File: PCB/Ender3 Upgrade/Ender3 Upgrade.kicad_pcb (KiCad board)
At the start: 2 copper layers, 95.5 x 118.9 mm, 1 part

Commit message: LED Wire Clip
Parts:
- removed ?: BuckConverter, albe:BuckConverter
- added DCDCBC1: DCDCBuckConverter, albe:BuckConverter, F.Cu at (81.5, 120.1)
- added REF**: TerminalBlock_bornier-2_P5.08mm, TerminalBlock:TerminalBlock_bornier-2_P5.08mm, F.Cu at (111.3, 53.8)
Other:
- board size 95.5 x 118.9 mm -> 46 x 110.7 mm
- board text added: "24V"
- board text added: "GND"
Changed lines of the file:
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@@
   (general
     (thickness 1.6)
-    (drawings 18)
+    (drawings 14)
     (tracks 0)
     (zones 0)
-    (modules 1)
-    (nets 1)
+    (modules 2)
+    (nets 5)
   )
   (page A4)
@@
     (pad_drill 0.762)
     (pad_to_mask_clearance 0)
-    (aux_axis_origin 0 0)
-    (grid_origin 134.874 113.03)
-    (visible_elements FFFFFD7F)
+    (aux_axis_origin 18.796 151.638)
+    (grid_origin 43.942 185.166)
+    (visible_elements 7FFFFFFF)
     (pcbplotparams
       (layerselection 0x010fc_ffffffff)
@@
   )
   (net 0 "")
+  (net 1 "Net-(DCDCBC1-Pad4)")
+  (net 2 "Net-(DCDCBC1-Pad3)")
+  (net 3 +24V)
+  (net 4 GND)
   (net_class Default "This is the default net class."
     (clearance 0.2)
@@
     (uvia_dia 0.3)
     (uvia_drill 0.1)
+    (add_net +24V)
+    (add_net GND)
+    (add_net "Net-(DCDCBC1-Pad3)")
+    (add_net "Net-(DCDCBC1-Pad4)")
   )
   (module albe:BuckConverter (layer F.Cu)
-    (at 129.032 79.756)
-    (fp_text reference "" (at 0 -22.36) (layer F.SilkS)
-      (effects (font (size 1 1) (thickness 0.15)))
-    )
-    (fp_text value BuckConverter (at 0 -23.36) (layer F.Fab)
+    (at 81.534 120.142)
+    (fp_text reference DCDCBC1 (at 0 -22.36) (layer F.SilkS)
+      (effects (font (size 1 1) (thickness 0.15)))
+    )
+    (fp_text value DCDCBuckConverter (at 0 -23.36) (layer F.Fab)
       (effects (font (size 1 1) (thickness 0.15)))
     )
@@
     (fp_line (start 0 -10.16) (end 5.08 -5.08) (layer F.SilkS) (width 0.12))
     (fp_line (start 5.08 -5.08) (end 3.81 -5.08) (layer F.SilkS) (width 0.12))
-    (pad 4 thru_hole circle (at -8.939073 -19.398813) (size 2 2) (drill 0.762) (layers *.Cu *.Mask))
-    (pad 3 thru_hole circle (at 8.89 -19.398813) (size 2 2) (drill 0.762) (layers *.Cu *.Mask))
-    (pad 2 thru_hole circle (at -8.939073 20.801187) (size 2 2) (drill 0.762) (layers *.Cu *.Mask))
-    (pad 1 thru_hole circle (at 8.910927 20.801187) (size 2 2) (drill 0.762) (layers *.Cu *.Mask))
-  )
-  (gr_line (start 69.596 41.91) (end 84.665419 42.231605) (layer Edge.Cuts) (width 0.05))
-  (gr_line (start 69.596 160.782) (end 69.596 41.91) (layer Edge.Cuts) (width 0.05))
-  (gr_line (start 164.846 160.782) (end 69.596 160.782) (layer Edge.Cuts) (width 0.05))
-  (gr_line (start 165.146 160.782) (end 164.846 160.782) (layer Edge.Cuts) (width 0.05))
-  (gr_line (start 165.146 68.95) (end 165.146 160.782) (layer Edge.Cuts) (width 0.05))
-  (gr_circle (center 107.696 94.5) (end 106.296 94.5) (layer Dwgs.User) (width 0.2))
-  (gr_arc (start 150.146 145.95) (end 150.146 160.95) (angle -18.1761416) (layer Dwgs.User) (width 0.2))
-  (gr_line (start 84.665419 160.95) (end 150.146 160.95) (layer Dwgs.User) (width 0.2))
-  (gr_arc (start 84.665419 145.95) (end 69.665419 145.95) (angle -90) (layer Dwgs.User) (width 0.2))
-  (gr_arc (start 84.665419 57.231605) (end 84.665419 42.231605) (angle -90) (layer Dwgs.User) (width 0.2))
-  (gr_line (start 150.146 42.231605) (end 84.665419 42.231605) (layer Edge.Cuts) (width 0.2))
-  (gr_line (start 168.146 68.95) (end 165.146 68.95) (layer Dwgs.User) (width 0.2))
-  (gr_circle (center 156.596 94.5) (end 155.196 94.5) (layer Dwgs.User) (width 0.2))
-  (gr_circle (center 156.596 152.4) (end 155.196 152.4) (layer Dwgs.User) (width 0.2))
-  (gr_arc (start 150.146 57.231605) (end 165.146 57.231605) (angle -90) (layer Edge.Cuts) (width 0.2))
-  (gr_line (start 165.146 68.95) (end 165.146 57.231605) (layer Edge.Cuts) (width 0.2))
-  (gr_line (start 69.665419 57.231605) (end 69.665419 145.95) (layer Dwgs.User) (width 0.2))
-  (gr_circle (center 107.696 152.4) (end 106.296 152.4) (layer Dwgs.User) (width 0.2))
+    (pad 4 thru_hole circle (at -8.939073 -19.398813) (size 2 2) (drill 0.762) (layers *.Cu *.Mask)
+      (net 1 "Net-(DCDCBC1-Pad4)"))
+    (pad 3 thru_hole circle (at 8.89 -19.398813) (size 2 2) (drill 0.762) (layers *.Cu *.Mask)
+      (net 2 "Net-(DCDCBC1-Pad3)"))
+    (pad 2 thru_hole circle (at -8.939073 20.801187) (size 2 2) (drill 0.762) (layers *.Cu *.Mask)
+      (net 3 +24V))
+    (pad 1 thru_hole circle (at 8.910927 20.801187) (size 2 2) (drill 0.762) (layers *.Cu *.Mask)
+      (net 4 GND))
+  )
+  (module TerminalBlock:TerminalBlock_bornier-2_P5.08mm (layer F.Cu)
+    (at 111.252 53.848 90)
+    (descr "simple 2-pin terminal block, pitch 5.08mm, revamped version of bornier2")
+    (tags "terminal block bornier2")
+    (fp_text reference REF** (at 2.54 -5.08 90) (layer F.SilkS)
+      (effects (font (size 1 1) (thickness 0.15)))
+    )
+    (fp_text value TerminalBlock_bornier-2_P5.08mm (at 2.54 5.08 90) (layer F.Fab)
+      (effects (font (size 1 1) (thickness 0.15)))
+    )
+    (fp_text user %R (at 2.54 0 90) (layer F.Fab)
+      (effects (font (size 1 1) (thickness 0.15)))
+    )
+    (fp_line (start -2.41 2.55) (end 7.49 2.55) (layer F.Fab) (width 0.1))
+    (fp_line (start -2.46 -3.75) (end -2.46 3.75) (layer F.Fab) (width 0.1))
+    (fp_line (start -2.46 3.75) (end 7.54 3.75) (layer F.Fab) (width 0.1))
+    (fp_line (start 7.54 3.75) (end 7.54 -3.75) (layer F.Fab) (width 0.1))
+    (fp_line (start 7.54 -3.75) (end -2.46 -3.75) (layer F.Fab) (width 0.1))
+    (fp_line (start 7.62 2.54) (end -2.54 2.54) (layer F.SilkS) (width 0.12))
+    (fp_line (start 7.62 3.81) (end 7.62 -3.81) (layer F.SilkS) (width 0.12))
+    (fp_line (start 7.62 -3.81) (end -2.54 -3.81) (layer F.SilkS) (width 0.12))
+    (fp_line (start -2.54 -3.81) (end -2.54 3.81) (layer F.SilkS) (width 0.12))
+    (fp_line (start -2.54 3.81) (end 7.62 3.81) (layer F.SilkS) (width 0.12))
+    (fp_line (start -2.71 -4) (end 7.79 -4) (layer F.CrtYd) (width 0.05))
+    (fp_line (start -2.71 -4) (end -2.71 4) (layer F.CrtYd) (width 0.05))
+    (fp_line (start 7.79 4) (end 7.79 -4) (layer F.CrtYd) (width 0.05))
+    (fp_line (start 7.79 4) (end -2.71 4) (layer F.CrtYd) (width 0.05))
+    (pad 2 thru_hole circle (at 5.08 0 90) (size 3 3) (drill 1.52) (layers *.Cu *.Mask))
+    (pad 1 thru_hole rect (at 0 0 90) (size 3 3) (drill 1.52) (layers *.Cu *.Mask))
+    (model ${KISYS3DMOD}/TerminalBlock.3dshapes/TerminalBlock_bornier-2_P5.08mm.wrl
+      (offset (xyz 2.539999961853027 0 0))
+      (scale (xyz 1 1 1))
+      (rotate (xyz 0 0 0))
+    )
+  )
+  (gr_line (start 70.026 141.374395) (end 70.026 52.656) (layer Edge.Cuts) (width 0.2))
+  (gr_arc (start 81.026 52.656) (end 81.026 41.656) (angle -90) (layer Edge.Cuts) (width 0.2))
+  (gr_text 24V (at 111.506 57.658) (layer F.SilkS)
+    (effects (font (size 1 1) (thickness 0.15)))
+  )
+  (gr_text GND (at 111.252 44.704) (layer F.SilkS)
+    (effects (font (size 1 1) (thickness 0.15)))
+  )
+  (gr_arc (start 114.026 43.656) (end 116.026 43.656) (angle -90) (layer Edge.Cuts) (width 0.2))
+  (gr_arc (start 86.026 147.374395) (end 86.026 152.374395) (angle -90) (layer Edge.Cuts) (width 0.2))
+  (gr_line (start 111.026 77.374395) (end 96.026 77.374395) (layer Edge.Cuts) (width 0.2))
+  (gr_line (start 116.026 43.656) (end 116.026 72.374395) (layer Edge.Cuts) (width 0.2))
+  (gr_line (start 91.026 82.374395) (end 91.026 147.374395) (layer Edge.Cuts) (width 0.2))
+  (gr_arc (start 81.026 141.374395) (end 70.026 141.374395) (angle -90) (layer Edge.Cuts) (width 0.2))
+  (gr_line (start 86.026 152.374395) (end 81.026 152.374395) (layer Edge.Cuts) (width 0.2))
+  (gr_arc (start 96.026 82.374395) (end 96.026 77.374395) (angle -90) (layer Edge.Cuts) (width 0.2))
+  (gr_arc (start 111.026 72.374395) (end 111.026 77.374395) (angle -90) (layer Edge.Cuts) (width 0.2))
+  (gr_line (start 81.026 41.656) (end 114.026 41.656) (layer Edge.Cuts) (width 0.2))
 )

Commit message: PCB Designed
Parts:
- removed the REF** at (111.3, 53.8)
- added C1: Conn_01x02, Connector_JST:JST_EH_B2B-EH-A_1x02_P2.50mm_Vertical, F.Cu at (131.8, 100.2)
- added C2: Conn_01x02, Connector_JST:JST_EH_B2B-EH-A_1x02_P2.50mm_Vertical, F.Cu at (160.3, 100.4)
- added C3: Conn_01x02, Connector_JST:JST_EH_B2B-EH-A_1x02_P2.50mm_Vertical, F.Cu at (143.7, 100.2)
- added C4: Conn_01x02, Connector_JST:JST_EH_B2B-EH-A_1x02_P2.50mm_Vertical, F.Cu at (172.2, 100.4)
- added C5: Conn_01x02, Connector_JST:JST_EH_B2B-EH-A_1x02_P2.50mm_Vertical, F.Cu at (141.2, 126.8)
- added C6: Conn_01x02, Connector_JST:JST_EH_B2B-EH-A_1x02_P2.50mm_Vertical, F.Cu at (169.7, 126.8)
- added C7: Conn_01x02, Connector_JST:JST_EH_B2B-EH-A_1x02_P2.50mm_Vertical, F.Cu at (129.3, 126.8)
- added C8: Conn_01x02, Connector_JST:JST_EH_B2B-EH-A_1x02_P2.50mm_Vertical, F.Cu at (157.7, 126.8)
- added DCDCBC2: DCDC 24-12, albe:BuckConverter, F.Cu at (99.8, 122.0)
- added J1 5V: Conn_01x04_Male, Connector_PinSocket_2.54mm:PinSocket_1x04_P2.54mm_Vertical, F.Cu at (140.2, 90.5)
- added J2 12V: Conn_01x04_Male, Connector_PinSocket_2.54mm:PinSocket_1x04_P2.54mm_Vertical, F.Cu at (161.0, 90.2)
- added R1: R1, Resistor_THT:R_Axial_DIN0204_L3.6mm_D1.6mm_P7.62mm_Horizontal, F.Cu at (126.7, 111.3)
- added R2: R1, Resistor_THT:R_Axial_DIN0204_L3.6mm_D1.6mm_P7.62mm_Horizontal, F.Cu at (155.2, 111.6)
- added R3: R1, Resistor_THT:R_Axial_DIN0204_L3.6mm_D1.6mm_P7.62mm_Horizontal, F.Cu at (138.7, 111.3)
- added R4: R1, Resistor_THT:R_Axial_DIN0204_L3.6mm_D1.6mm_P7.62mm_Horizontal, F.Cu at (167.1, 111.6)
- added R5: R1, Resistor_THT:R_Axial_DIN0204_L3.6mm_D1.6mm_P7.62mm_Horizontal, F.Cu at (146.3, 115.6)
- added R6: R1, Resistor_THT:R_Axial_DIN0204_L3.6mm_D1.6mm_P7.62mm_Horizontal, F.Cu at (174.7, 115.9)
- added R7: R1, Resistor_THT:R_Axial_DIN0204_L3.6mm_D1.6mm_P7.62mm_Horizontal, F.Cu at (134.3, 115.6)
- added R8: R1, Resistor_THT:R_Axial_DIN0204_L3.6mm_D1.6mm_P7.62mm_Horizontal, F.Cu at (162.8, 115.9)
- added REF**: MountingHole_2.2mm_M2_Pad, MountingHole:MountingHole_2.2mm_M2_Pad, F.Cu at (176.9, 87.9)
- added REF**: MountingHole_2.2mm_M2_Pad, MountingHole:MountingHole_2.2mm_M2_Pad, F.Cu at (176.7, 131.5)
- added REF**: MountingHole_2.2mm_M2_Pad, MountingHole:MountingHole_2.2mm_M2_Pad, F.Cu at (73.1, 131.6)
- added REF**: MountingHole_2.2mm_M2_Pad, MountingHole:MountingHole_2.2mm_M2_Pad, F.Cu at (73.4, 88.0)
- added T1: IRLZ34N, Package_TO_SOT_THT:TO-220-3_Vertical, F.Cu at (128.0, 107.2)
- added T2: IRLZ34N, Package_TO_SOT_THT:TO-220-3_Vertical, F.Cu at (156.5, 107.5)
- added T3: IRLZ34N, Package_TO_SOT_THT:TO-220-3_Vertical, F.Cu at (140.0, 107.2)
- added T4: IRLZ34N, Package_TO_SOT_THT:TO-220-3_Vertical, F.Cu at (168.4, 107.5)
- added T5: IRLZ34N, Package_TO_SOT_THT:TO-220-3_Vertical, F.Cu at (145.0, 119.8)
- added T6: IRLZ34N, Package_TO_SOT_THT:TO-220-3_Vertical, F.Cu at (173.4, 119.9)
- added T7: IRLZ34N, Package_TO_SOT_THT:TO-220-3_Vertical, F.Cu at (133.1, 119.8)
- added T8: IRLZ34N, Package_TO_SOT_THT:TO-220-3_Vertical, F.Cu at (161.5, 119.9)
- DCDCBC1: value DCDCBuckConverter -> DCDC 24-5
- moved DCDCBC1 28.8 mm to (99.8, 97.9), turned to 270 degrees
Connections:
- DCDCBC1 pad 1: GND -> GNDPWR
- DCDCBC1 pad 3: Net-(DCDCBC1-Pad3) -> GND
- DCDCBC1 pad 4: Net-(DCDCBC1-Pad4) -> 5V
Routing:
- net GND: track 0.00 -> 124.7 mm
- net 12V: track 0.00 -> 116.0 mm
- net 5V: track 0.00 -> 73.6 mm
- net Net-(J1-Pad1): track 0.00 -> 73.5 mm
- net Net-(J2-Pad4): track 0.00 -> 71.5 mm
- net Net-(J1-Pad2): track 0.00 -> 35.5 mm
- net Net-(J2-Pad3): track 0.00 -> 35.0 mm
- net +24V: track 0.00 -> 27.5 mm
- net GNDPWR: track 0.00 -> 27.5 mm
- net Net-(J2-Pad2): track 0.00 -> 23.9 mm
- net Net-(J2-Pad1): track 0.00 -> 23.7 mm
- net Net-(J1-Pad3): track 0.00 -> 23.6 mm
- net Net-(J1-Pad4): track 0.00 -> 23.4 mm
- net Net-(C3-Pad1): track 0.00 -> 7.58 mm
- net Net-(C1-Pad1): track 0.00 -> 7.58 mm
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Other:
- board size 46 x 110.7 mm -> 110 x 50 mm
- board text added: "1"
- board text added: "12V"
- board text added: "2"
- board text added: "3"
- board text added: "4"
- board text added: "5"
- board text added: "5V"
- board text added: "6"
- board text added: "7"
- board text added: "8"
- board text added: "Ideated and Designed by Alberto Rota"
- board text removed: "24V"
- board text removed: "GND"

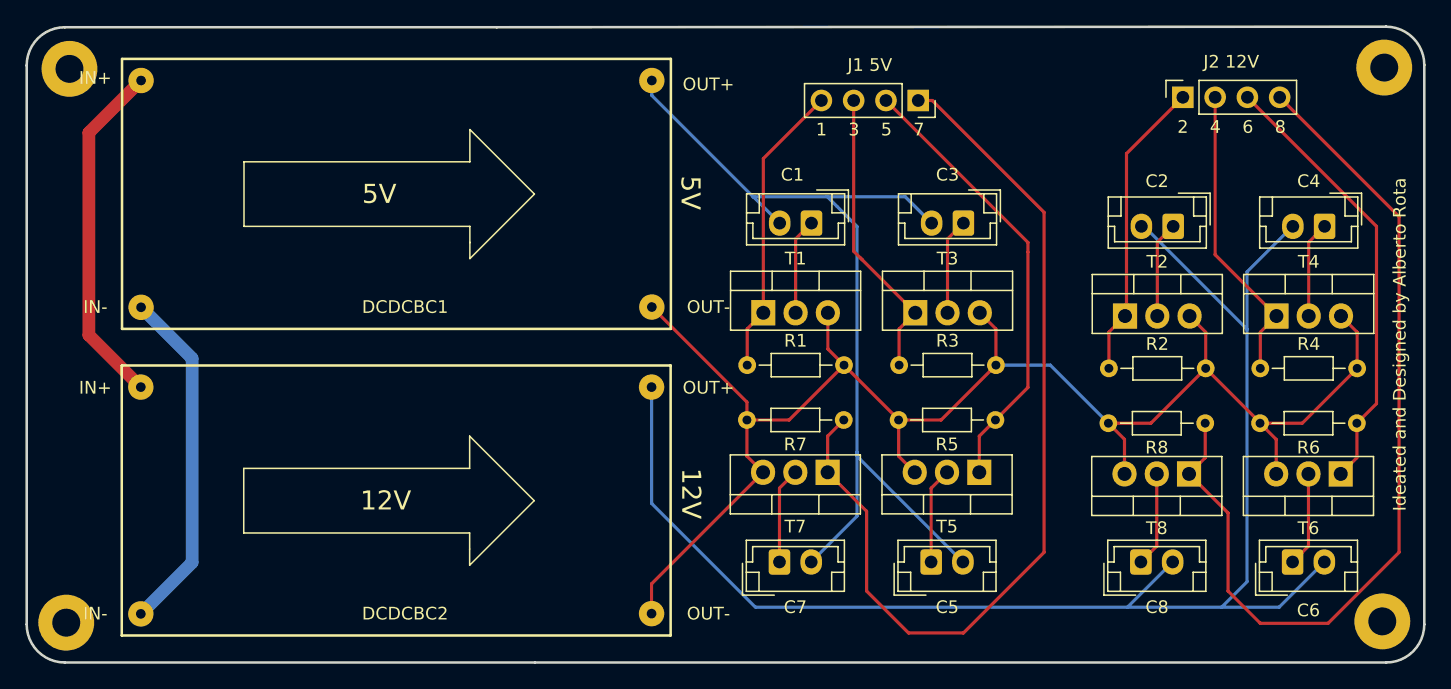
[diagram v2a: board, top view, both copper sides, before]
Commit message: Drawers added
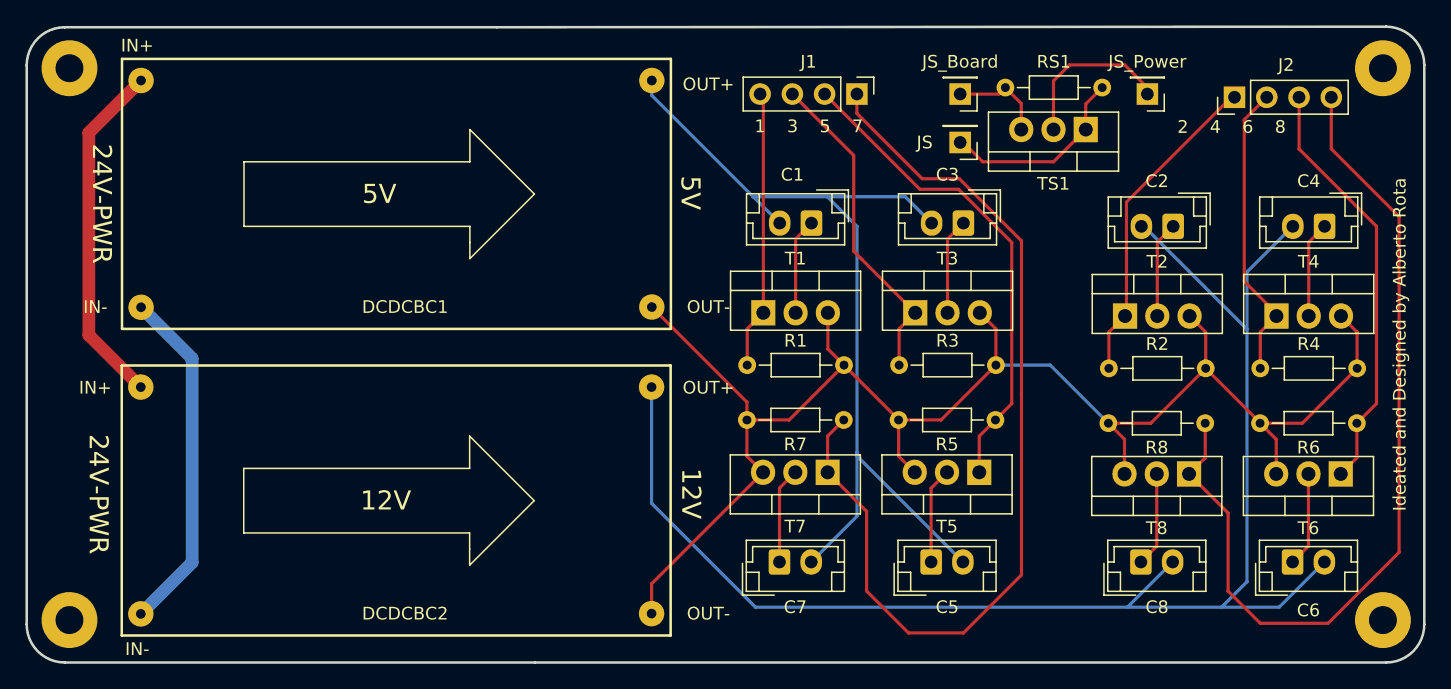
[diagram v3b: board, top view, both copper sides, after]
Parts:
- removed J1 5V: Conn_01x04_Male, Connector_PinSocket_2.54mm:PinSocket_1x04_P2.54mm_Vertical
- removed J2 12V: Conn_01x04_Male, Connector_PinSocket_2.54mm:PinSocket_1x04_P2.54mm_Vertical
- removed the REF** at (176.9, 87.9)
- removed the REF** at (176.7, 131.5)
- removed the REF** at (73.1, 131.6)
- added J1: Conn_01x04_Male, Connector_PinHeader_2.54mm:PinHeader_1x04_P2.54mm_Vertical, F.Cu at (135.4, 90.0)
- added J2: Conn_01x04_Male, Connector_PinHeader_2.54mm:PinHeader_1x04_P2.54mm_Vertical, F.Cu at (165.1, 90.2)
- added JS: Conn_01x01_Male, Connector_PinHeader_2.54mm:PinHeader_1x01_P2.54mm_Vertical, F.Cu at (143.5, 93.8)
- added JS_Board: Conn_01x01_Male, Connector_PinHeader_2.54mm:PinHeader_1x01_P2.54mm_Vertical, F.Cu at (143.5, 90.0)
- added JS_Power: Conn_01x01_Male, Connector_PinHeader_2.54mm:PinHeader_1x01_P2.54mm_Vertical, F.Cu at (158.2, 90.0)
- added REF**: MountingHole_2.2mm_M2_Pad, MountingHole:MountingHole_2.2mm_M2_Pad, F.Cu at (176.8, 88.0)
- added REF**: MountingHole_2.2mm_M2_Pad, MountingHole:MountingHole_2.2mm_M2_Pad, F.Cu at (176.8, 131.4)
- added REF**: MountingHole_2.2mm_M2_Pad, MountingHole:MountingHole_2.2mm_M2_Pad, F.Cu at (73.4, 131.4)
- added RS1: R1, Resistor_THT:R_Axial_DIN0204_L3.6mm_D1.6mm_P7.62mm_Horizontal, F.Cu at (154.7, 89.5)
- added TS1: IRLZ34N, Package_TO_SOT_THT:TO-220-3_Vertical, F.Cu at (153.4, 92.8)
- moved REF** 0.05 mm to (73.4, 88.0)
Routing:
- net Net-(JS_Control1-Pad1): track 0.00 -> 15.4 mm
- net Net-(JS_Power1-Pad1): track 0.00 -> 13.0 mm
- net Net-(JS_Board1-Pad1): track 0.00 -> 7.59 mm
- net Net-(J1-Pad2): track 35.5 -> 38.7 mm
- net Net-(J1-Pad3): track 23.6 -> 26.1 mm
- net Net-(J1-Pad1): track 73.5 -> 75.7 mm
- net Net-(J2-Pad1): track 23.7 -> 25.6 mm
- net Net-(J2-Pad4): track 71.5 -> 69.9 mm
- net Net-(J2-Pad3): track 35.0 -> 33.3 mm
- net Net-(J1-Pad4): track 23.4 -> 22.1 mm
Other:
- board text added: "24V-PWR"
